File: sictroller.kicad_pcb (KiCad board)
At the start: 2 copper layers, 152.4 x 92.5 mm, 98 parts, among them J1 CONN_01X08, J10 CONN_01X03, J11 CONN_01X03, J12 CONN_02X13, J2 CONN_01X12, J3 TMDSCNCD28069, J4 CONN_01X03, J5 BARREL_JACK, J6 CONN_02X05, J7 CONN_01X02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

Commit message: Add test points; PCB connectors placed
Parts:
- added W10: TEST_1P, Measurement_Points:Measurement_Point_Round-SMD-Pad_Small, F.Cu at (252.6, 17.8)
- added W11: TEST_1P, Measurement_Points:Measurement_Point_Round-SMD-Pad_Small, F.Cu at (265.8, 3.50)
- added W12: TEST_1P, Measurement_Points:Measurement_Point_Round-SMD-Pad_Small, F.Cu at (259.2, 17.8)
- added W13: TEST_1P, Measurement_Points:Measurement_Point_Round-SMD-Pad_Small, F.Cu at (265.8, 10.6)
- added W14: TEST_1P, Measurement_Points:Measurement_Point_Round-SMD-Pad_Small, F.Cu at (245.9, 3.50)
- added W15: TEST_1P, Measurement_Points:Measurement_Point_Round-SMD-Pad_Small, F.Cu at (272.5, 10.6)
- added W16: TEST_1P, Measurement_Points:Measurement_Point_Round-SMD-Pad_Small, F.Cu at (265.8, 17.8)
- added W17: TEST_1P, Measurement_Points:Measurement_Point_Round-SMD-Pad_Small, F.Cu at (279.1, 3.50)
- added W18: TEST_1P, Measurement_Points:Measurement_Point_Round-TH_Small, F.Cu at (273.8, 17.8)
- added W19: TEST_1P, Measurement_Points:Measurement_Point_Round-TH_Small, F.Cu at (287.0, 3.50)
- added W20: TEST_1P, Measurement_Points:Measurement_Point_Round-SMD-Pad_Small, F.Cu at (279.1, 10.6)
- added W21: TEST_1P, Measurement_Points:Measurement_Point_Round-SMD-Pad_Small, F.Cu at (285.8, 10.6)
- added W22: TEST_1P, Measurement_Points:Measurement_Point_Round-SMD-Pad_Small, F.Cu at (279.1, 17.8)
- added W23: TEST_1P, Measurement_Points:Measurement_Point_Round-SMD-Pad_Small, F.Cu at (285.8, 17.8)
- added W3: TEST_1P, Measurement_Points:Measurement_Point_Round-TH_Small, F.Cu at (273.8, 3.50)
- added W4: TEST_1P, Measurement_Points:Measurement_Point_Round-TH_Small, F.Cu at (247.2, 10.6)
- added W5: TEST_1P, Measurement_Points:Measurement_Point_Round-TH_Small, F.Cu at (253.8, 3.50)
- added W6: TEST_1P, Measurement_Points:Measurement_Point_Round-TH_Small, F.Cu at (247.2, 17.8)
- added W7: TEST_1P, Measurement_Points:Measurement_Point_Round-TH_Small, F.Cu at (260.5, 3.50)
- added W8: TEST_1P, Measurement_Points:Measurement_Point_Round-TH_Small, F.Cu at (253.8, 10.6)
- added W9: TEST_1P, Measurement_Points:Measurement_Point_Round-TH_Small, F.Cu at (260.5, 10.6)
- J1: footprint Connectors_Molex:Connector_Molex_PicoBlade_53398-0871 -> Connectors_Molex:Connector_Molex_PicoBlade_53261-0871
- J2: footprint Connectors_Molex:Connector_Molex_PicoBlade_53398-1271 -> Connectors_Molex:Connector_Molex_PicoBlade_53261-1271; moved to B.Cu
- moved J8 364.3 mm to (215.9, 79.8), turned to 270 degrees
- moved J11 346.3 mm to (215.9, 121.7), turned to 270 degrees
- moved J7 343.8 mm to (209.6, 72.6)
- moved J9 334.8 mm to (215.9, 93.7), turned to 270 degrees
- moved J10 328.9 mm to (215.9, 107.7), turned to 270 degrees
- moved J6 323.1 mm to (184.4, 69.1), turned to 180 degrees
- moved J5 259.8 mm to (198.6, 145.0), turned to 90 degrees
- moved J3 258.1 mm to (132.8, 103.6)
- moved R2 251.6 mm to (192.0, 138.4), turned to 90 degrees
- moved D1 249.4 mm to (96.0, 132.3)
- moved J2 240.1 mm to (78.2, 105.7), turned to 90 degrees
- moved R1 232.8 mm to (108.0, 127.5), turned to 180 degrees
- moved U2 231.0 mm to (178.6, 118.4), turned to 90 degrees
- moved W2 228.6 mm to (120.9, 98.0)
- moved C4 228.5 mm to (187.2, 127.3), turned to 90 degrees
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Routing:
- added copper zone on In1.Cu, net GND
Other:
- copper layers 2 -> 4

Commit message: Change J6 (microfit) pinning for better routing of HV
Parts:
- moved R20 388.6 mm to (241.5, 110.0)
- moved R21 388.6 mm to (241.5, 103.7)
- moved C10 366.2 mm to (262.4, 106.3)
- moved C12 366.2 mm to (295.3, 93.7)
- moved C13 366.2 mm to (270.1, 120.6)
- moved C14 366.2 mm to (281.7, 107.0)
- moved C15 366.2 mm to (262.3, 98.8)
- moved C17 366.2 mm to (276.7, 118.6)
- moved C18 366.2 mm to (302.5, 97.4)
- moved C19 366.2 mm to (298.9, 93.7)
- moved C20 366.2 mm to (295.6, 112.8)
- moved C22 366.2 mm to (277.3, 112.7)
- moved C24 366.2 mm to (288.0, 101.1)
- moved C7 366.2 mm to (292.8, 107.0)
- moved C8 366.2 mm to (280.8, 112.8)
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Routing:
- added copper zone on In2.Cu, net +5VA

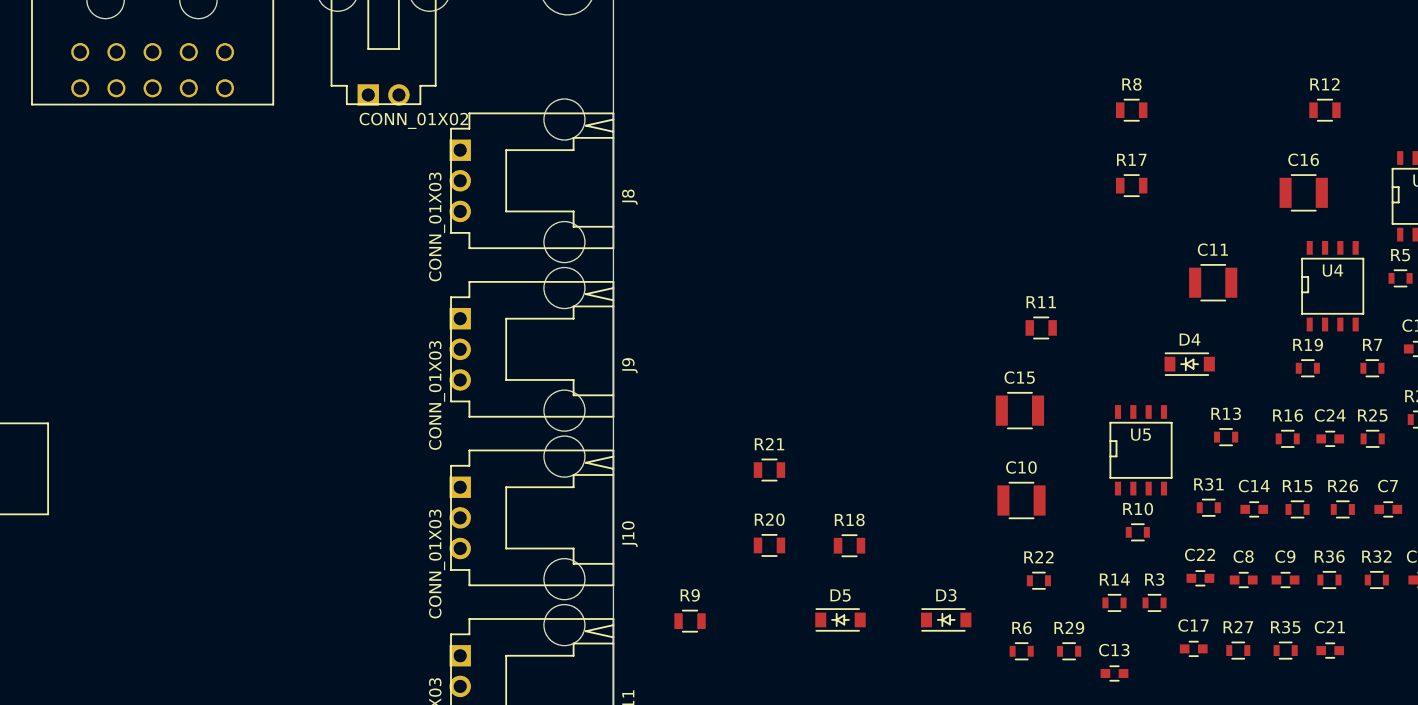
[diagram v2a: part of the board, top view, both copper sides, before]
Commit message: Change J6 (microfit) pinning for better routing of HV
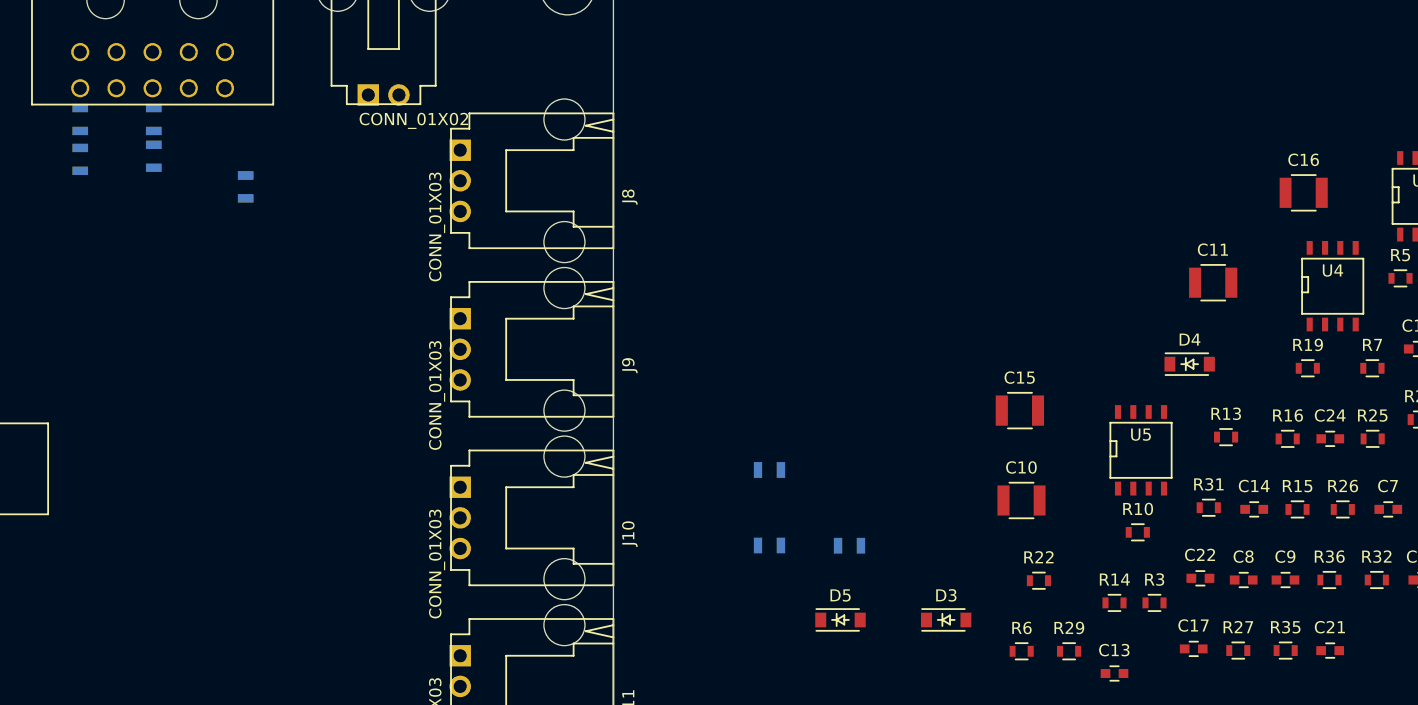
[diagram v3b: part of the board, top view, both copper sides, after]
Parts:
- J6: value CONN_02X05 -> MICROFIT-10
- R11, R12, R17, R18, R20, R21, R8, R9: moved to B.Cu
- moved R12 103.3 mm to (184.4, 78.0), turned to 90 degrees
- moved R11 81.5 mm to (184.4, 74.7), turned to 90 degrees
- moved R8 81.1 mm to (190.5, 74.7), turned to 90 degrees
- moved R17 73.4 mm to (198.1, 80.3), turned to 270 degrees
- moved R9 58.8 mm to (190.5, 77.7), turned to 90 degrees
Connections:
- J6 pad 1: /Feedback/HV- -> /Feedback/PWR_TEMP_IN
- J6 pad 10: /Feedback/PWR_TEMP_IN -> /Feedback/HV-
- J6 pad 2: /Feedback/HV+ -> /Feedback/VsL_A
- J6 pad 3: /Feedback/VsL_A -> /Feedback/VsL_B
- J6 pad 4: /Feedback/PHASE_A -> /Feedback/VsL_C
- J6 pad 5: /Feedback/VsL_B -> GND
- J6 pad 6: /Feedback/PHASE_B -> /Feedback/HV+
- J6 pad 7: /Feedback/VsL_C -> /Feedback/PHASE_A
- J6 pad 8: /Feedback/PHASE_C -> /Feedback/PHASE_B
- J6 pad 9: GND -> /Feedback/PHASE_C
- W10 pad 1: Net-(W10-Pad1) -> /Control Card/VFB_B
- W11 pad 1: Net-(W11-Pad1) -> /Control Card/IFB_B
- W12 pad 1: Net-(W12-Pad1) -> /Control Card/Vds_B
- W13 pad 1: Net-(W13-Pad1) -> /Control Card/VFB_C
- W14 pad 1: Net-(W14-Pad1) -> /Control Card/IFB_C
- W15 pad 1: Net-(W15-Pad1) -> /Control Card/Vds_C
- W16 pad 1: Net-(W16-Pad1) -> /Control Card/VFB_BUS
- W17 pad 1: Net-(W17-Pad1) -> /Control Card/IFB_BUS
- W7 pad 1: Net-(W7-Pad1) -> /Control Card/Vds_A
- W8 pad 1: Net-(W8-Pad1) -> /Control Card/VFB_A
- W9 pad 1: Net-(W9-Pad1) -> /Control Card/IFB_A

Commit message: Most parts placed-ish
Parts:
- R3: moved to B.Cu
- moved W3 239.3 mm to (59.4, 109.8)
- moved W5 210.9 mm to (69.9, 106.6)
- moved W4 209.3 mm to (61.3, 106.7)
- moved W19 204.2 mm to (117.1, 116.8)
- moved W6 202.9 mm to (67.1, 111.3)
- moved W21 195.3 mm to (122.0, 117.1)
- moved W20 191.3 mm to (120.0, 116.6)
- moved W23 186.9 mm to (127.2, 116.7)
- moved W18 186.8 mm to (115.1, 116.5)
- moved W22 183.5 mm to (124.7, 116.8)
- moved R19 173.3 mm to (112.8, 95.2), turned to 270 degrees
- moved C11 168.7 mm to (109.7, 92.2), turned to 180 degrees
- moved C16 167.9 mm to (118.6, 95.4)
- moved R13 166.8 mm to (112.8, 92.1), turned to 270 degrees
- moved R10 157.6 mm to (115.4, 92.1), turned to 270 degrees
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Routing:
- added copper zone on In2.Cu, net +5VD
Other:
- board text added: "Conformal coat req'd for creepage"

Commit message: Swap level shifter pins for easier routing
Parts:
- moved U7 17.0 mm to (104.1, 127.4)
- moved R37 13.3 mm to (115.8, 127.8), turned to 270 degrees
- moved U6 5.08 mm to (107.6, 137.4), turned to 270 degrees
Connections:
- net Net-(J12-Pad7) renamed /Gate driver board/PWM_BL_TTL
- J12 pad 1: Net-(J12-Pad1) -> /Gate driver board/PWM_AH_TTL
- J12 pad 11: Net-(J12-Pad11) -> /Gate driver board/PWM_CL_TTL
- J12 pad 13: Net-(J12-Pad13) -> /Gate driver board/~PWR_RESET_TTL
- J12 pad 3: Net-(J12-Pad3) -> /Gate driver board/PWM_AL_TTL
- J12 pad 5: Net-(J12-Pad5) -> /Gate driver board/PWM_BH_TTL
- J12 pad 9: Net-(J12-Pad9) -> /Gate driver board/PWM_CH_TTL
- U6 pad 15: Net-(J12-Pad13) -> /Gate driver board/PWM_AH_TTL
- U6 pad 16: Net-(J12-Pad11) -> /Gate driver board/PWM_AL_TTL
- U6 pad 17: Net-(J12-Pad9) -> /Gate driver board/PWM_BH_TTL
- U6 pad 19: Net-(J12-Pad5) -> /Gate driver board/PWM_CH_TTL
- U6 pad 20: Net-(J12-Pad3) -> /Gate driver board/PWM_CL_TTL
- U6 pad 21: Net-(J12-Pad1) -> /Gate driver board/~PWR_RESET_TTL
- U6 pad 3: /Control Card/PWM_AH -> /Control Card/~PWR_RESET
- U6 pad 4: /Gate driver board/PWM_AL -> /Control Card/PWM_CL
- U6 pad 5: /Gate driver board/PWM_BH -> /Control Card/PWM_BL
- U6 pad 7: /Control Card/PWM_BL -> /Gate driver board/PWM_BH
- U6 pad 8: /Control Card/PWM_CL -> /Gate driver board/PWM_AL
- U6 pad 9: /Control Card/~PWR_RESET -> /Control Card/PWM_AH

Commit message: About to start routing
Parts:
- J2, R3: moved to F.Cu
- moved W6 137.3 mm to (204.0, 121.5)
- moved W4 120.4 mm to (180.3, 89.2)
- moved W5 102.0 mm to (169.4, 129.3)
- moved W3 58.0 mm to (114.9, 126.3)
- moved W7 44.9 mm to (125.3, 110.1)
- moved W15 37.9 mm to (129.6, 110.0)
- moved C2 34.0 mm to (166.5, 134.9), turned to 180 degrees
- moved W12 31.4 mm to (127.6, 110.2)
- moved W14 30.1 mm to (133.1, 81.0)
- moved C6 23.2 mm to (122.4, 131.8)
- moved U7 21.8 mm to (122.3, 139.6)
- moved W13 19.2 mm to (113.3, 85.5)
- moved C25 17.6 mm to (112.6, 135.1), turned to 270 degrees
- moved J2 17.5 mm to (78.3, 88.2), turned to 270 degrees
- moved C26 16.8 mm to (112.6, 139.6), turned to 90 degrees
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
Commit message: Started routing
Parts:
- moved R34 45.3 mm to (194.8, 101.9), turned to 180 degrees
- moved D5 44.2 mm to (198.6, 101.9)
- moved D1 4.70 mm to (89.3, 131.4), turned to 180 degrees
- moved Q1 2.05 mm to (91.9, 122.7), turned to 180 degrees
- moved C1 0.51 mm to (152.7, 146.1)
- moved C26 0.18 mm to (112.8, 139.4), turned to 270 degrees
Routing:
- net +15V: track 0.00 -> 100.2 mm
- net Net-(D1-Pad1): track 0.00 -> 16.0 mm
- net /Gate driver board/~PWR_RESET_TTL: track 0.00 -> 13.4 mm
- net Net-(D1-Pad3): track 0.00 -> 12.4 mm
- net /Gate driver board/PWM_CL_TTL: track 0.00 -> 11.7 mm
- net /Gate driver board/PWM_AH_TTL: track 0.00 -> 10.4 mm
- net /Gate driver board/PWM_CH_TTL: track 0.00 -> 10.0 mm
- net GND: track 0.00 -> 9.76 mm, vias 0 -> 5
- net /Gate driver board/PWM_AL_TTL: track 0.00 -> 9.65 mm
- net /Gate driver board/PWM_BL_TTL: track 0.00 -> 9.24 mm
- net /Gate driver board/PWM_BH_TTL: track 0.00 -> 8.86 mm
- net +5VD: track 0.00 -> 5.09 mm, vias 0 -> 1
- net Net-(J4-Pad1): track 0.00 -> 3.56 mm
- net Net-(J3-Pad90): track 0.00 -> 3.14 mm
- net Net-(J3-Pad91): track 0.00 -> 2.58 mm
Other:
- net class +15V added: clearance 0.1524, trace_width 0.8128, via_dia 0.635, via_drill 0.254
- net class Default: clearance 0.2 -> 0.1524; trace_width 0.25 -> 0.1524; via_dia 0.8 -> 0.635; via_drill 0.4 -> 0.254
- net class HV added: clearance 0.254, trace_width 0.1524, via_dia 0.635, via_drill 0.254
- net class Logic power added: clearance 0.1524, trace_width 0.3048, via_dia 0.635, via_drill 0.254
- rule trace_clearance: 0.2 -> 0.1524
- rule trace_min: 0.2 -> 0.127
- rule via_min_drill: 0.3 -> 0.254
- rule via_min_size: 0.4 -> 0.635

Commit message: routing, but weird netnames on PWM
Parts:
- moved C5 49.2 mm to (124.6, 134.4)
- moved W18 15.1 mm to (103.0, 125.5)
- moved W19 13.5 mm to (105.5, 123.8)
- moved C6 4.47 mm to (118.0, 132.7)
- moved U2 4.34 mm to (121.3, 132.8)
- moved C27 4.10 mm to (119.3, 137.8), turned to 270 degrees
- moved R39 1.73 mm to (119.3, 140.8)
- moved R37 1.02 mm to (107.8, 128.1)
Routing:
- net +3V3: track 0.00 -> 19.3 mm
- net GND: track 9.76 -> 25.7 mm, vias 5 -> 16
- net /Control Card/~PWR_RESET: track 0.00 -> 13.8 mm
- net /Control Card/PWM_AH: track 0.00 -> 13.2 mm
- net /Gate driver board/PWM_AL: track 0.00 -> 13.0 mm
- net /Gate driver board/PWM_BH: track 0.00 -> 12.9 mm
- net /Control Card/PWR_RDY: track 0.00 -> 12.6 mm
- net +5VD: track 5.09 -> 17.6 mm, vias 1 -> 5
- net /Control Card/PWM_CL: track 0.00 -> 12.2 mm
- net /Gate driver board/FLT_OTP_TTL: track 0.00 -> 8.35 mm
- net /Gate driver board/FLT_DESAT_TTL: track 0.00 -> 7.96 mm
- net /Gate driver board/PWR_RDY_TTL: track 0.00 -> 7.16 mm
- net /Control Card/~FLT_DESAT: track 0.00 -> 4.73 mm
- net /Control Card/~FLT_OTP: track 0.00 -> 1.98 mm
